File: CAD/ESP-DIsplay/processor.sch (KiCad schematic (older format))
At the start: 0 parts

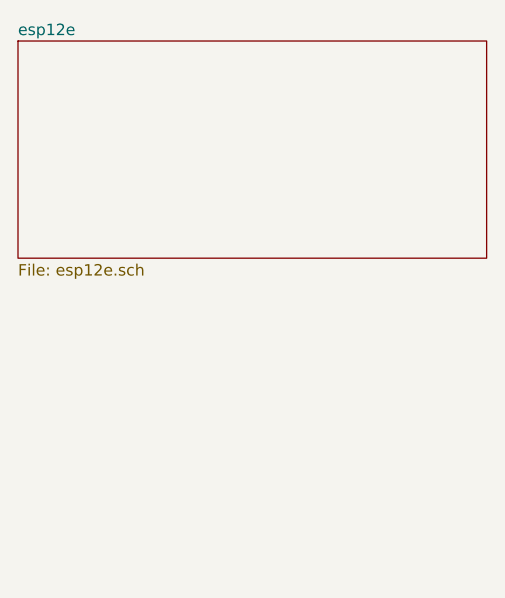
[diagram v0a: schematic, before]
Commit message: ESP32 added
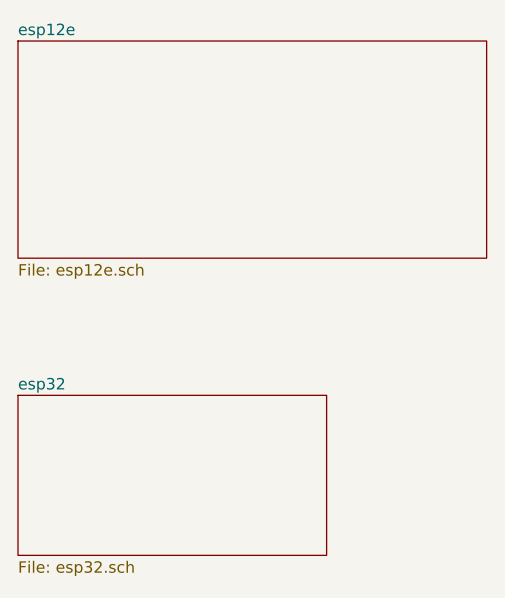
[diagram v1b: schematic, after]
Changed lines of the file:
@@
 $Descr A4 11693 8268
 encoding utf-8
-Sheet 2 8
+Sheet 2 9
 Title ""
 Date ""
@@
 F1 "esp12e.sch" 50
 $EndSheet
+$Sheet
+S 6850 4350 1350 700
+U 608F83B4
+F0 "esp32" 50
+F1 "esp32.sch" 50
+$EndSheet
 $EndSCHEMATC

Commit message: ESP Display v1
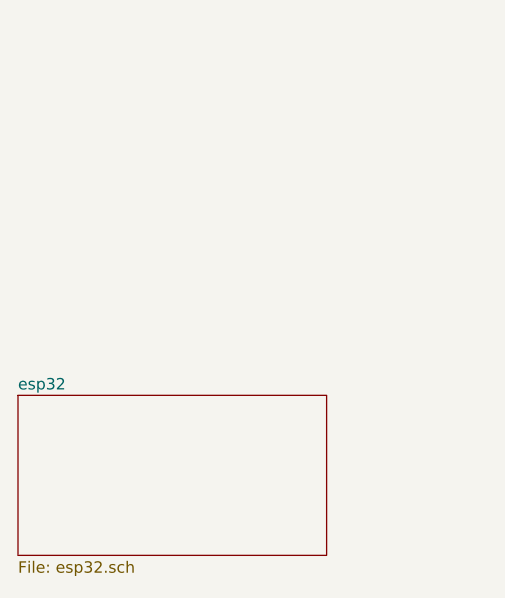
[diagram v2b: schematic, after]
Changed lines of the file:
@@
 $Descr A4 11693 8268
 encoding utf-8
-Sheet 2 9
+Sheet 2 8
 Title ""
 Date ""
@@
 $EndDescr
 $Sheet
-S 6850 2800 2050 950
-U 60B1EE3B
-F0 "esp12e" 50
-F1 "esp12e.sch" 50
-$EndSheet
-$Sheet
 S 6850 4350 1350 700
